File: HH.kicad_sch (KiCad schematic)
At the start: 11 parts

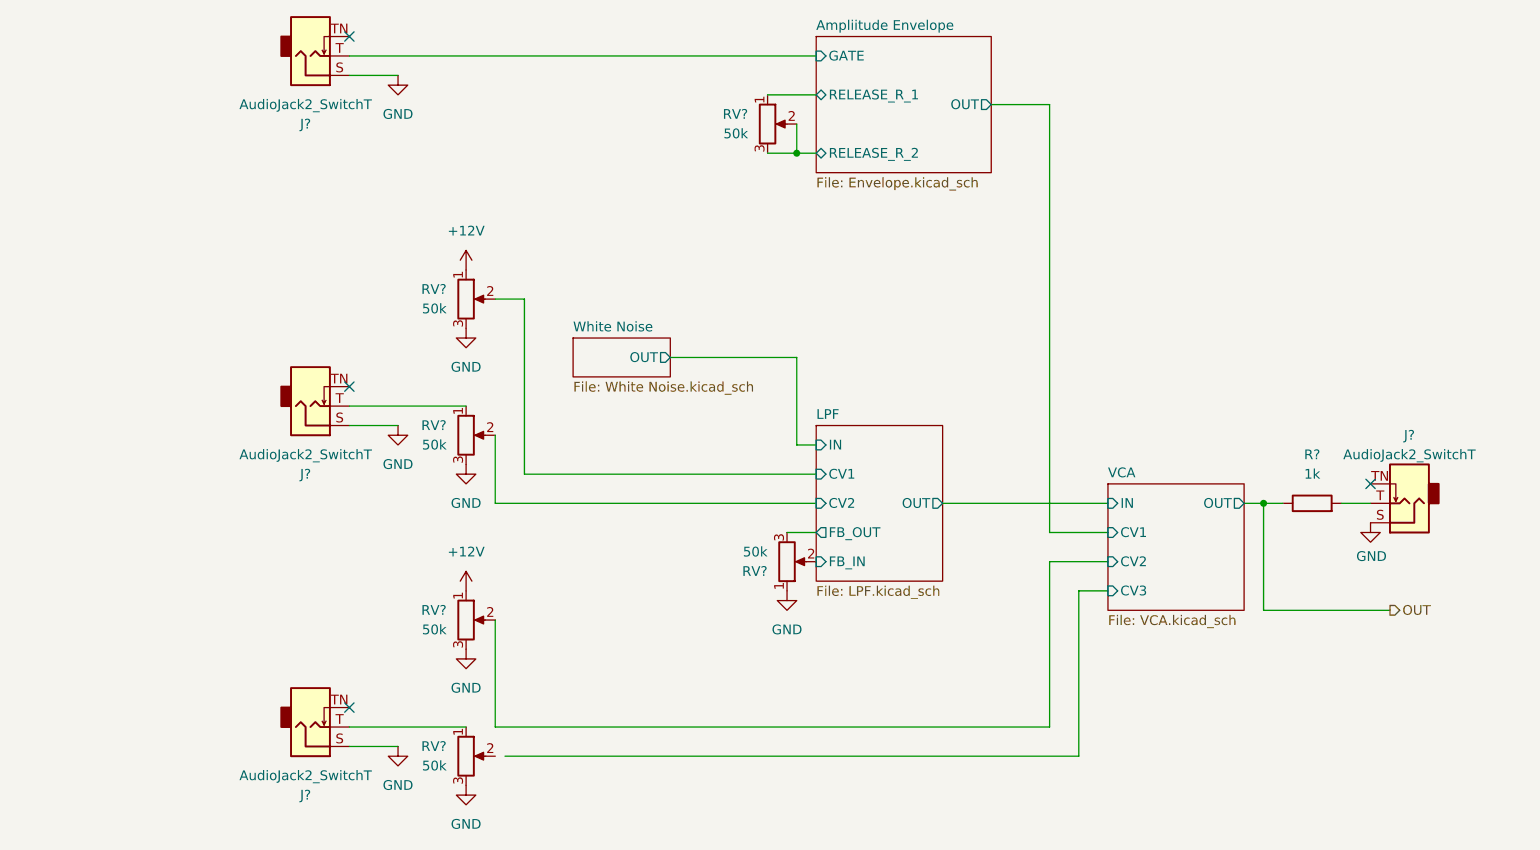
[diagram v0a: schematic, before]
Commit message: Finish schematic
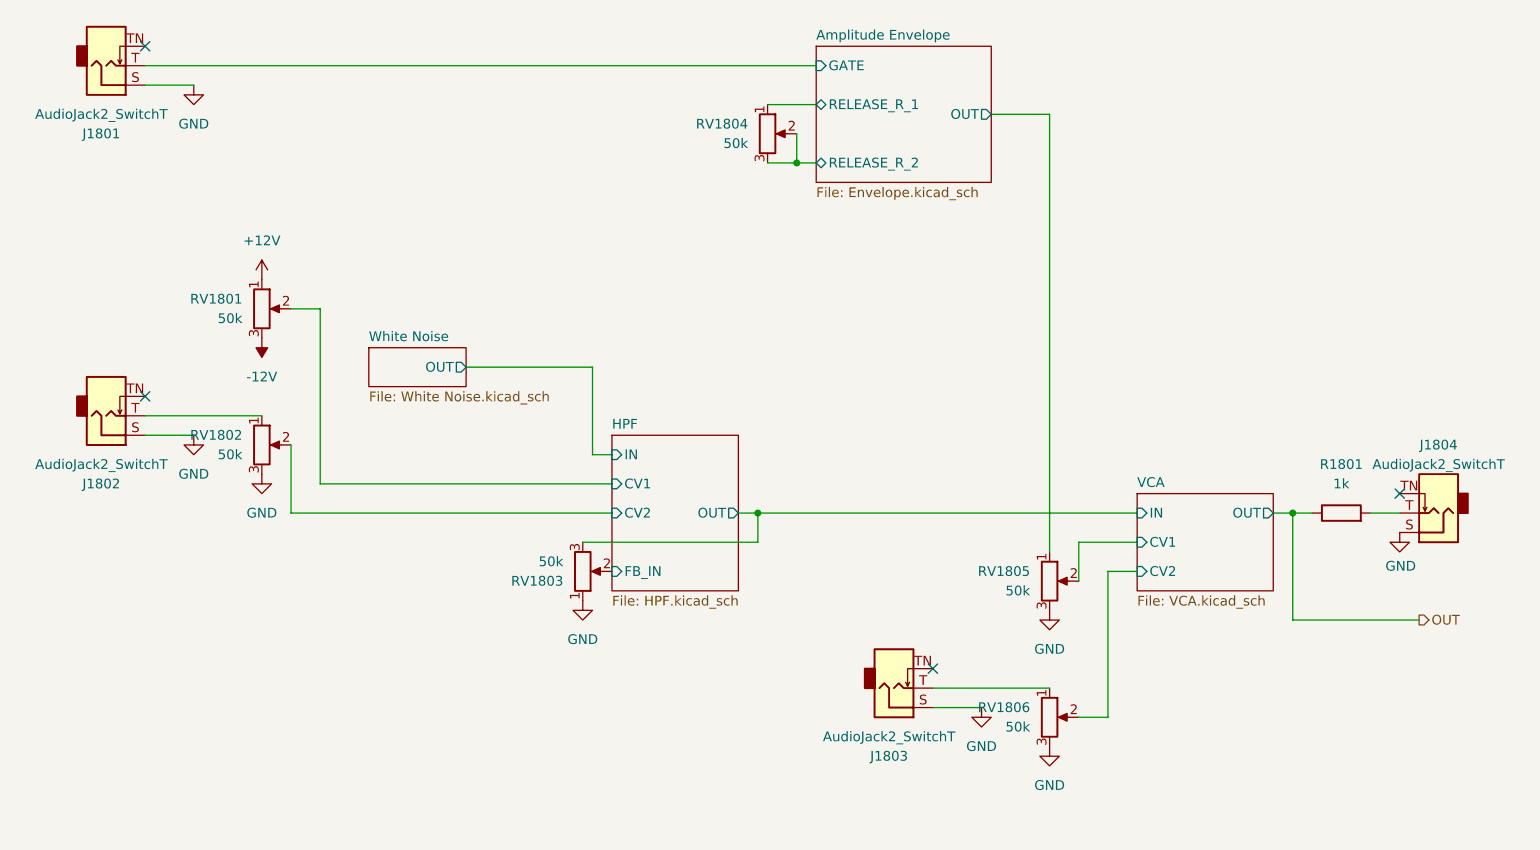
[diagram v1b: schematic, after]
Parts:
- removed J?: AudioJack2_SwitchT, symbol Connector:AudioJack2_SwitchT
- removed RV? (x2): 50k, symbol Device:R_Potentiometer
- added J1803: AudioJack2_SwitchT, Connector_Audio:Jack_3.5mm_QingPu_WQP-PJ398SM_Vertical_CircularHoles, symbol Connector:AudioJack2_SwitchT
- added RV1805, RV1806: 50k, Potentiometer_THT:Potentiometer_Alpha_RD901F-40-00D_Single_Vertical_CircularHoles, symbol Device:R_Potentiometer
- J1801, J1802: renamed from J?; footprint (none) -> Connector_Audio:Jack_3.5mm_QingPu_WQP-PJ398SM_Vertical_CircularHoles
- R1801: renamed from R?; footprint (none) -> Resistor_THT:R_Axial_DIN0207_L6.3mm_D2.5mm_P7.62mm_Horizontal
- RV1801, RV1802, RV1803, RV1804: renamed from RV?; footprint (none) -> Potentiometer_THT:Potentiometer_Alpha_RD901F-40-00D_Single_Vertical_CircularHoles
- gave numbers to parts that had none: 1
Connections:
- net HPF/FB_OUT is gone; now on net HPF/OUT: RV1803.3
- net Amplitude Envelope/OUT: now also RV1805.1
- net GND: now also J1803.S, RV1805.3, RV1806.3; no longer RV1801.3
- net VCA/CV2: now also RV1806.2
- new net: J1803.T, RV1806.1
- new net -12V: RV1801.3
- new net VCA/CV1: RV1805.2
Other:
- sheet Ampliitude Envelope renamed Amplitude Envelope
- sheet LPF renamed HPF
- sheet HPF: file LPF.kicad_sch -> HPF.kicad_sch
- sheet HPF ports: added none; removed FB_OUT
- sheet VCA ports: added none; removed CV3
- moved on the sheet: J1801, J1802, J1804, R1801, RV1801, RV1802, RV1803, RV1804
